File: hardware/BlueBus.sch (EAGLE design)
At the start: 76 parts

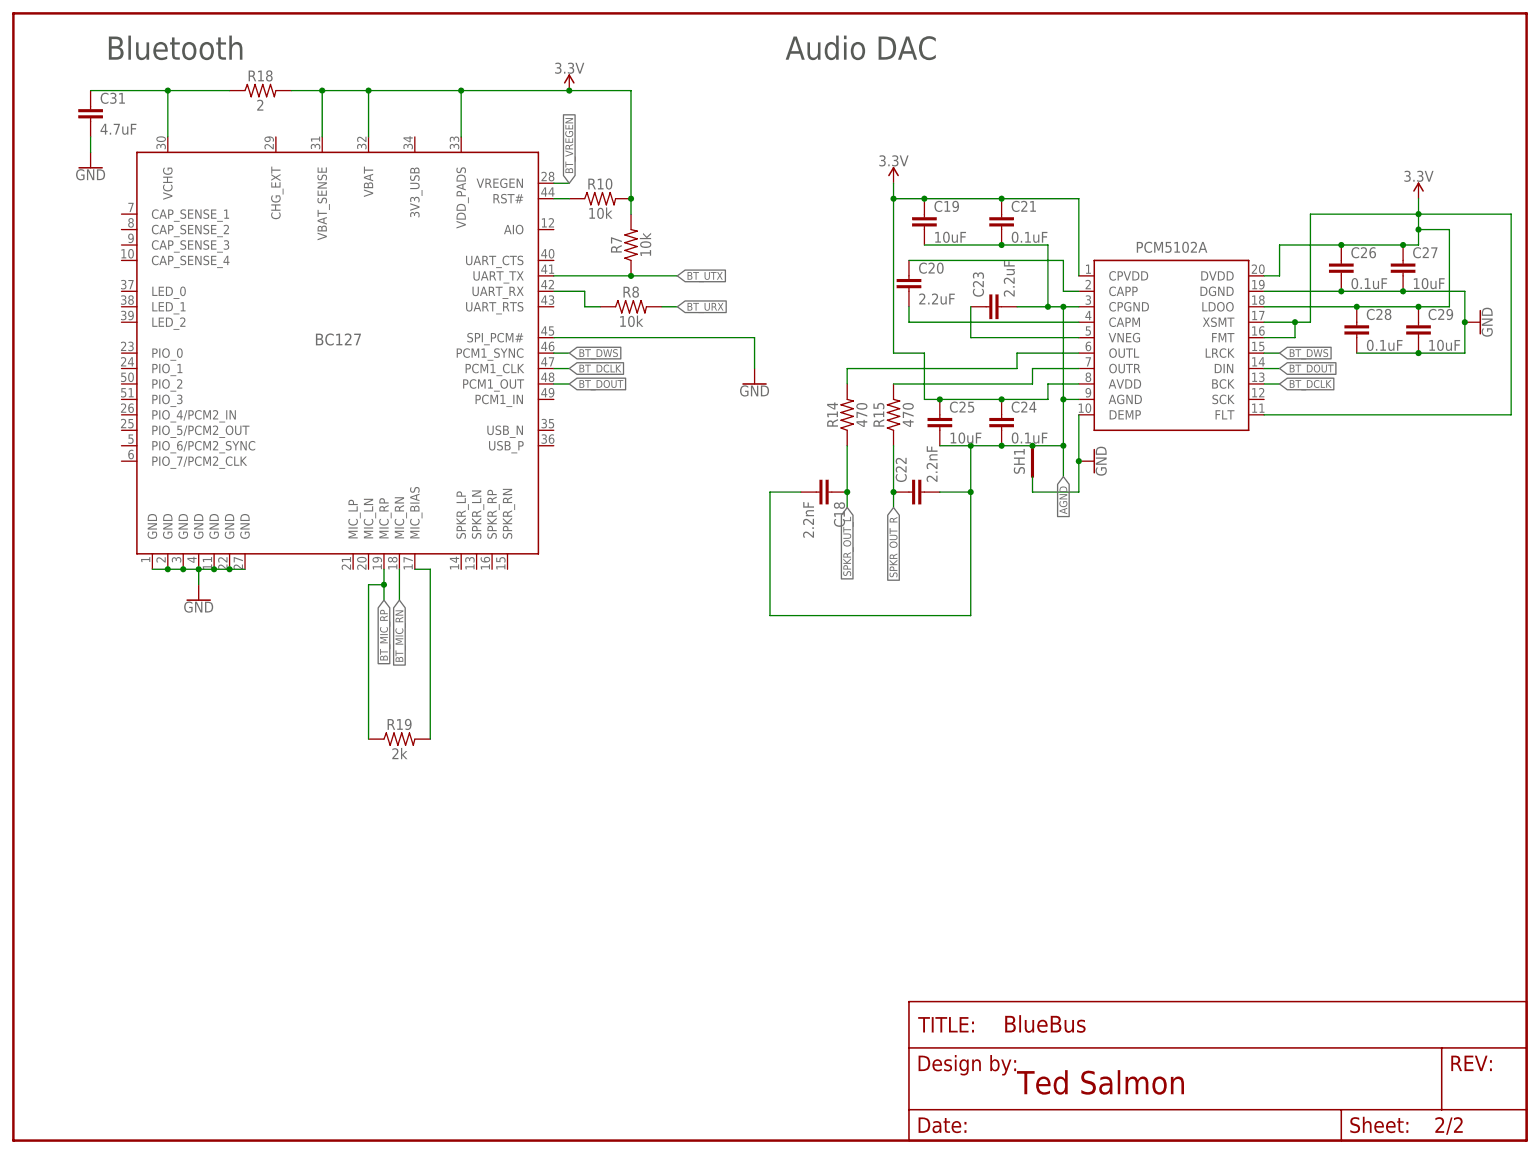
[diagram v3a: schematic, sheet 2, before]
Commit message: [IMP] hardware: BlueBus Rev A * Improve Silkscreen * Rewire a couple of nets to reduce via count * Move passives into better alignment
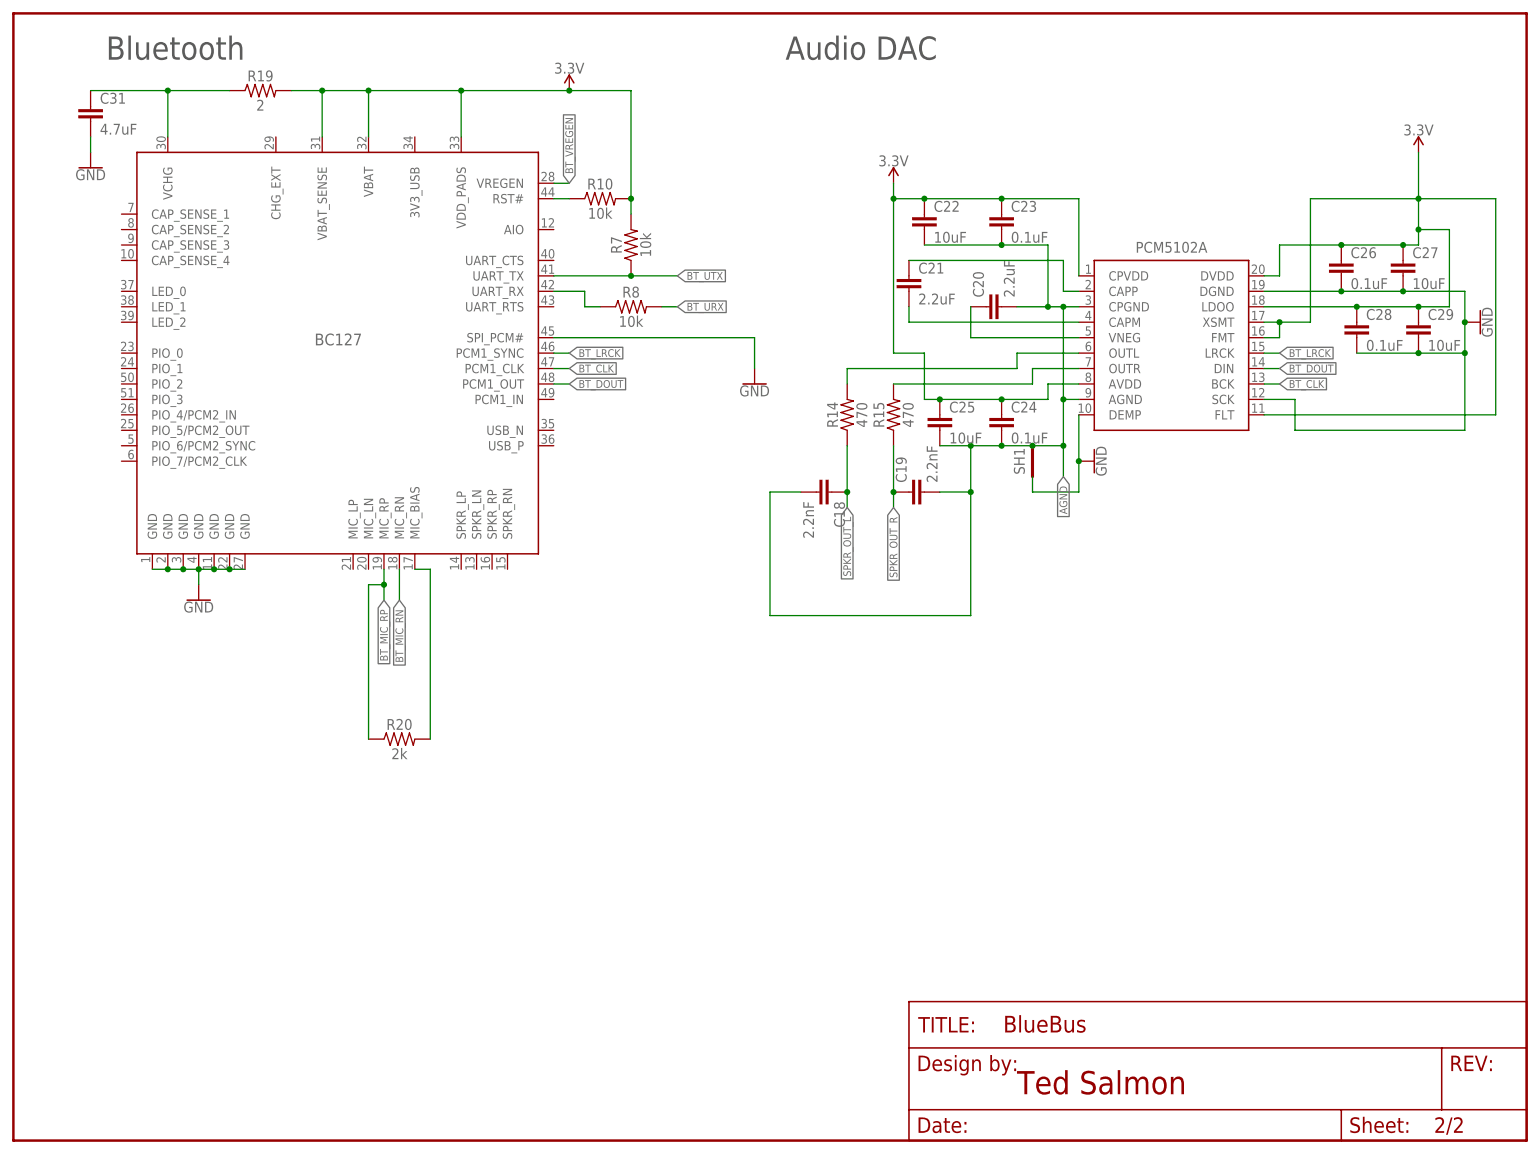
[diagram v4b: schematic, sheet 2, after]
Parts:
- removed R16: 10k, Passives:10KOHM
- added R20: 2k, Passives:2KOHM
- C19: value 10uF -> 2.2nF; device Passives:10UF2012 -> Passives:2.2NF
- C21: value 0.1uF -> 2.2uF; device Passives:0.1UF -> Passives:2.2UF
- C22: value 2.2nF -> 10uF; device Passives:2.2NF -> Passives:10UF2012
- C23: value 2.2uF -> 0.1uF; device Passives:2.2UF -> Passives:0.1UF
- R17: value 240 -> 10k; device Passives:240OHM -> Passives:10KOHM
- R18: value 2 -> 240; device Passives:2OHM -> Passives:240OHM
- R19: value 2k -> 2; device Passives:2KOHM -> Passives:2OHM
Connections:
- net BT_DCLK renamed BT_CLK
- net BT_DWS renamed BT_LRCK
- net 3.3V: now also C22.1, C23.1, R17.1, R19.2; no longer C19.1, C21.1, R16.1, R18.2
- net AGND: now also C20.2; no longer C21.2
- net BT_3V3_FILTER: now also R19.1; no longer R18.1
- net BT_MIC_BIAS: now also R20.2; no longer R19.2
- net BT_MIC_RP: now also R20.1; no longer R19.1
- net DAC_CAPM: now also C21.2; no longer C20.2
- net DAC_CAPP: now also C21.1; no longer C20.1
- net DAC_VNEG: now also C20.1; no longer C23.1
- net GND: now also PCM5102A.SCK
- net MCU_MCLR: now also R18.2; no longer R17.2
- net MCU_MCLR_RES: now also R17.2, R18.1; no longer R16.2, R17.1
- net SPKR_OUT_R: now also C19.1; no longer C22.1
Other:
- moved on the sheet: C19, C20, C21, C22, C23, R17, R19

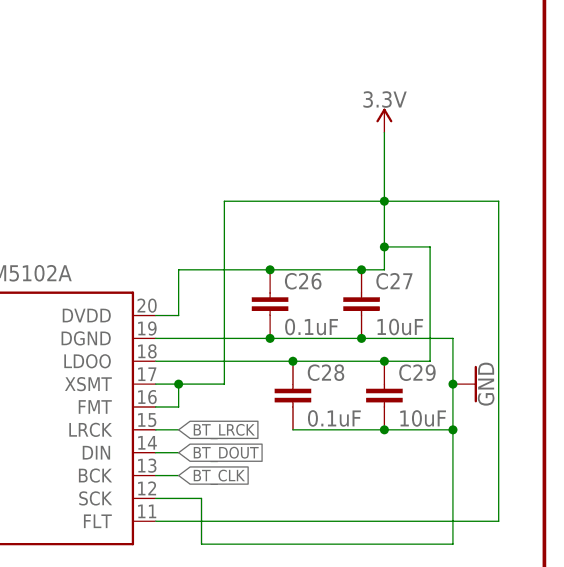
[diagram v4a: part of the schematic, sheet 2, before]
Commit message: [IMP] hardware: PCM5102AQ1 fixes * Remove +3.3 from LDOO caps * Wire XSMT & FMT back to +3.3 * Rewire feedback pin of +5v switching regulator
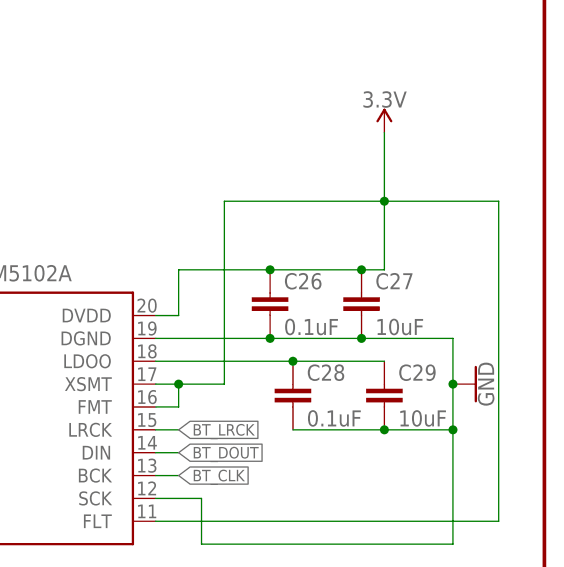
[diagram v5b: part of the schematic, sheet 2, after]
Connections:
- new net LDOO: C28.1, C29.1, PCM5102A.LDOO
- net 3.3V: no longer C28.1, C29.1, PCM5102A.LDOO
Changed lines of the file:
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@@
 <?xml version="1.0" encoding="utf-8"?>
 <!DOCTYPE eagle SYSTEM "eagle.dtd">
-<eagle version="9.2.2">
+<eagle version="9.3.0">
 <drawing>
 <settings>
@@
 <pinref part="C27" gate="G$1" pin="1"/>
 <wire x1="231.14" y1="162.56" x2="231.14" y2="154.94" width="0.1524" layer="91"/>
-<wire x1="231.14" y1="154.94" x2="231.14" y2="149.86" width="0.1524" layer="91"/>
-<wire x1="231.14" y1="149.86" x2="231.14" y2="147.32" width="0.1524" layer="91"/>
+<wire x1="231.14" y1="154.94" x2="231.14" y2="147.32" width="0.1524" layer="91"/>
 <wire x1="231.14" y1="147.32" x2="228.6" y2="147.32" width="0.1524" layer="91"/>
 <pinref part="C26" gate="G$1" pin="1"/>
@@
 <pinref part="PCM5102A" gate="G$1" pin="DVDD"/>
 <wire x1="208.28" y1="142.24" x2="205.74" y2="142.24" width="0.1524" layer="91"/>
-<pinref part="PCM5102A" gate="G$1" pin="LDOO"/>
-<pinref part="C28" gate="G$1" pin="1"/>
-<wire x1="205.74" y1="137.16" x2="220.98" y2="137.16" width="0.1524" layer="91"/>
-<pinref part="C29" gate="G$1" pin="1"/>
-<wire x1="220.98" y1="137.16" x2="231.14" y2="137.16" width="0.1524" layer="91"/>
-<junction x="220.98" y="137.16"/>
-<wire x1="231.14" y1="137.16" x2="236.22" y2="137.16" width="0.1524" layer="91"/>
-<wire x1="236.22" y1="137.16" x2="236.22" y2="149.86" width="0.1524" layer="91"/>
-<junction x="231.14" y="137.16"/>
-<wire x1="236.22" y1="149.86" x2="231.14" y2="149.86" width="0.1524" layer="91"/>
-<junction x="231.14" y="149.86"/>
 <wire x1="231.14" y1="154.94" x2="213.36" y2="154.94" width="0.1524" layer="91"/>
 <wire x1="213.36" y1="154.94" x2="213.36" y2="134.62" width="0.1524" layer="91"/>
@@
 </segment>
 </net>
+<net name="LDOO" class="2">
+<segment>
+<pinref part="C29" gate="G$1" pin="1"/>
+<pinref part="C28" gate="G$1" pin="1"/>
+<wire x1="220.98" y1="137.16" x2="231.14" y2="137.16" width="0.1524" layer="91"/>
+<junction x="220.98" y="137.16"/>
+<pinref part="PCM5102A" gate="G$1" pin="LDOO"/>
+<wire x1="205.74" y1="137.16" x2="220.98" y2="137.16" width="0.1524" layer="91"/>
+</segment>
+</net>
